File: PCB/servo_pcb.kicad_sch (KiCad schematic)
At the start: 31 parts, among them J1 power in, M1 M1, M2 M2, U1 MM32G0001, U2 SL7533-3, U3 BDR6121H, U4 INA180A2, U5 AS5600

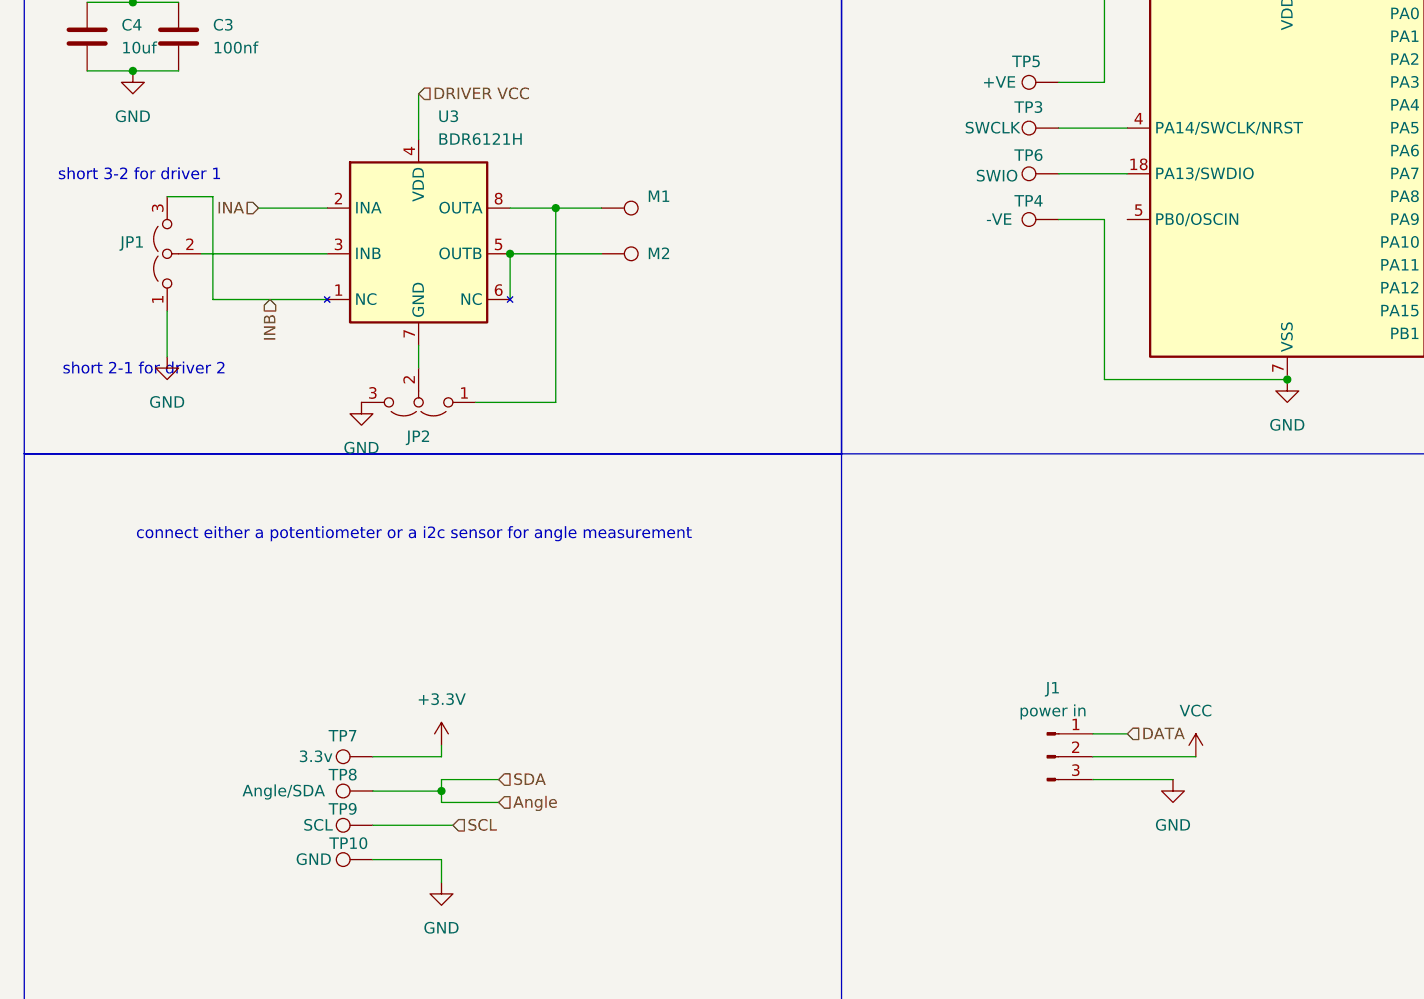
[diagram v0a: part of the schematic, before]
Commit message: Cleaned up PCB folder and updated readme, updated pcb
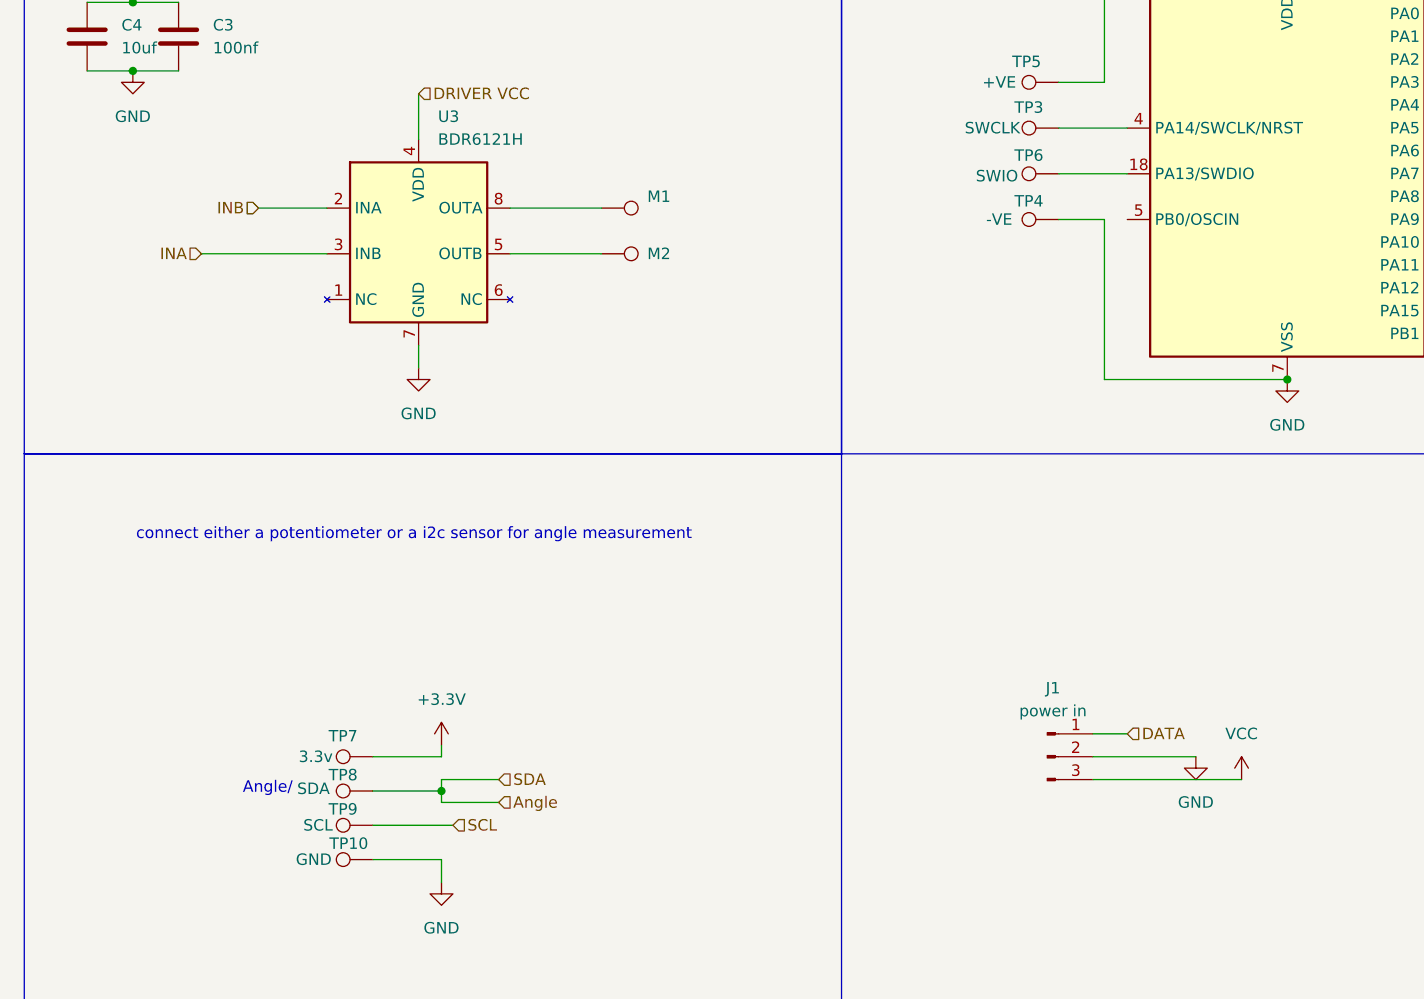
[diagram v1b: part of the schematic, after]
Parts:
- removed JP1, JP2: ~, Jumper:SolderJumper-3_P1.3mm_Open_Pad1.0x1.5mm, symbol Jumper:Jumper_3_Open
- TP8: value Angle/SDA -> SDA
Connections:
- net GND: now also J1.2 (Pin_2), U3.7 (GND); no longer J1.3 (Pin_3)
- net INA: now also U3.3 (INB); no longer U3.2 (INA)
- net INB: now also U3.2 (INA); no longer U3.1 (NC)
- net VCC: now also J1.3 (Pin_3); no longer J1.2 (Pin_2)
- net at M2.1, U3.5 (OUTB): no longer U3.6 (NC)
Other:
- note added: "Angle/"
- note removed: "short 2-1 for driver 2"
- note removed: "short 3-2 for driver 1"
